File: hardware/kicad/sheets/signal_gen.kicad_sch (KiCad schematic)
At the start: 32 parts, among them U11 SG-8002CA-PH 25MHz, U12 AD9833BRMZ, U13 OPA1656ID, U14 AD633JRZ-R7, U15 MCP4921-E/SN, U16 LM4040DBZ-2.5, U17 OPA188ID

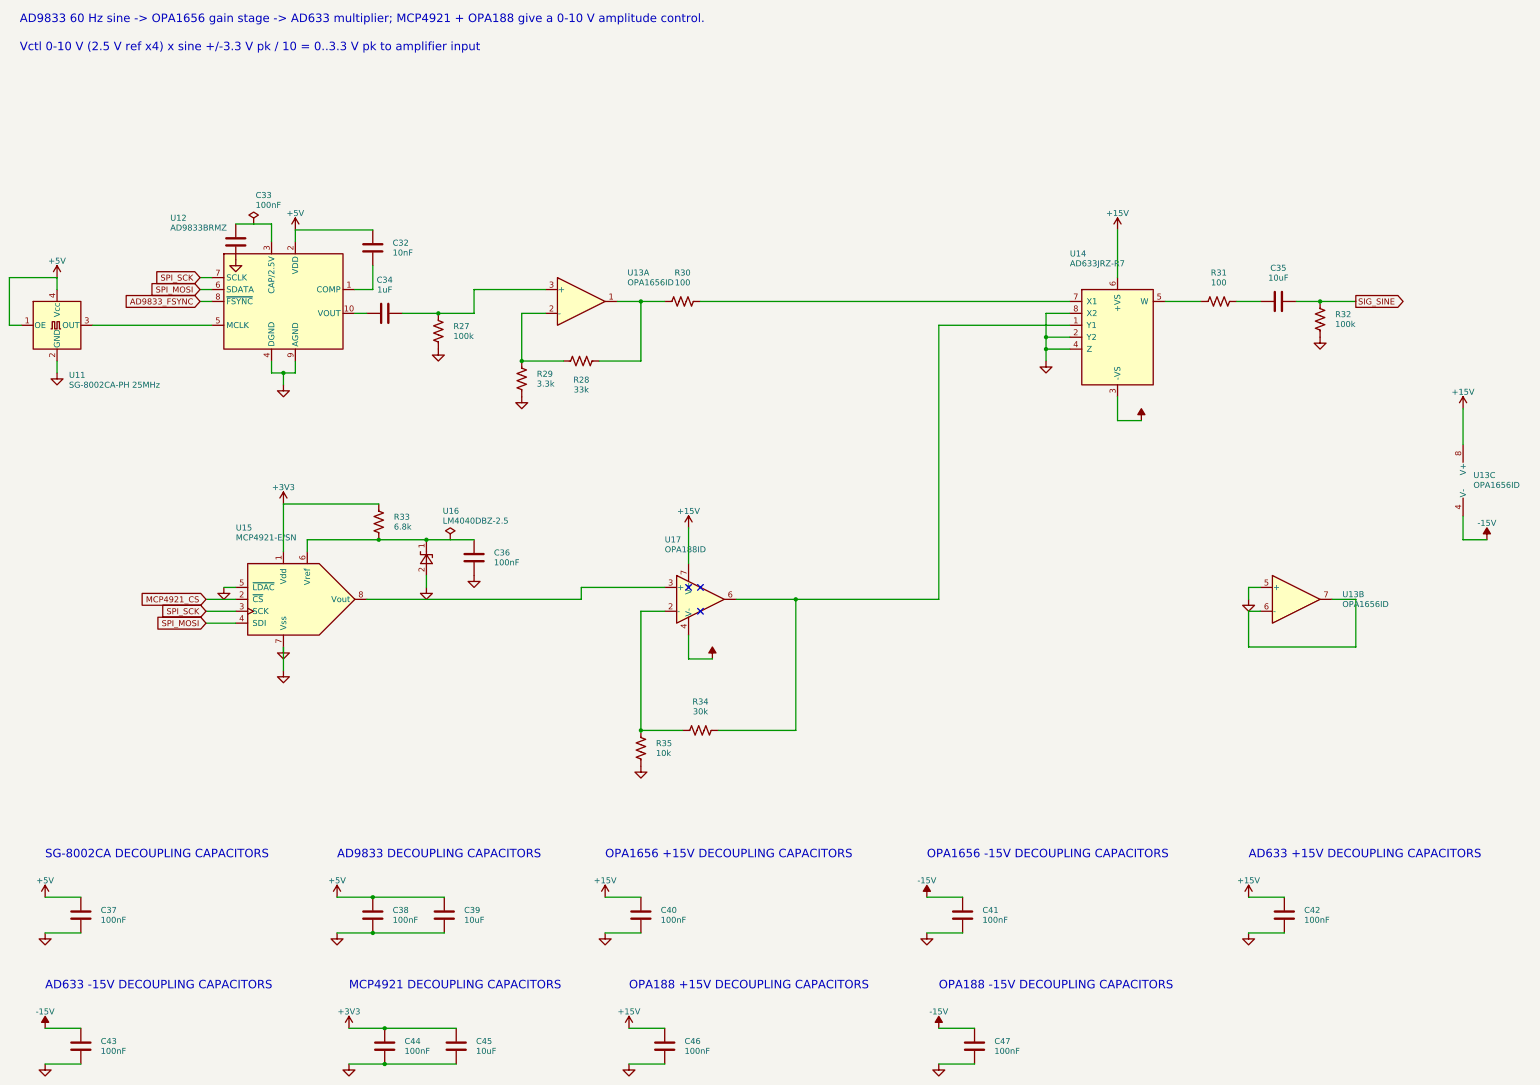
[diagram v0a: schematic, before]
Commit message: Fixing the UUID issues
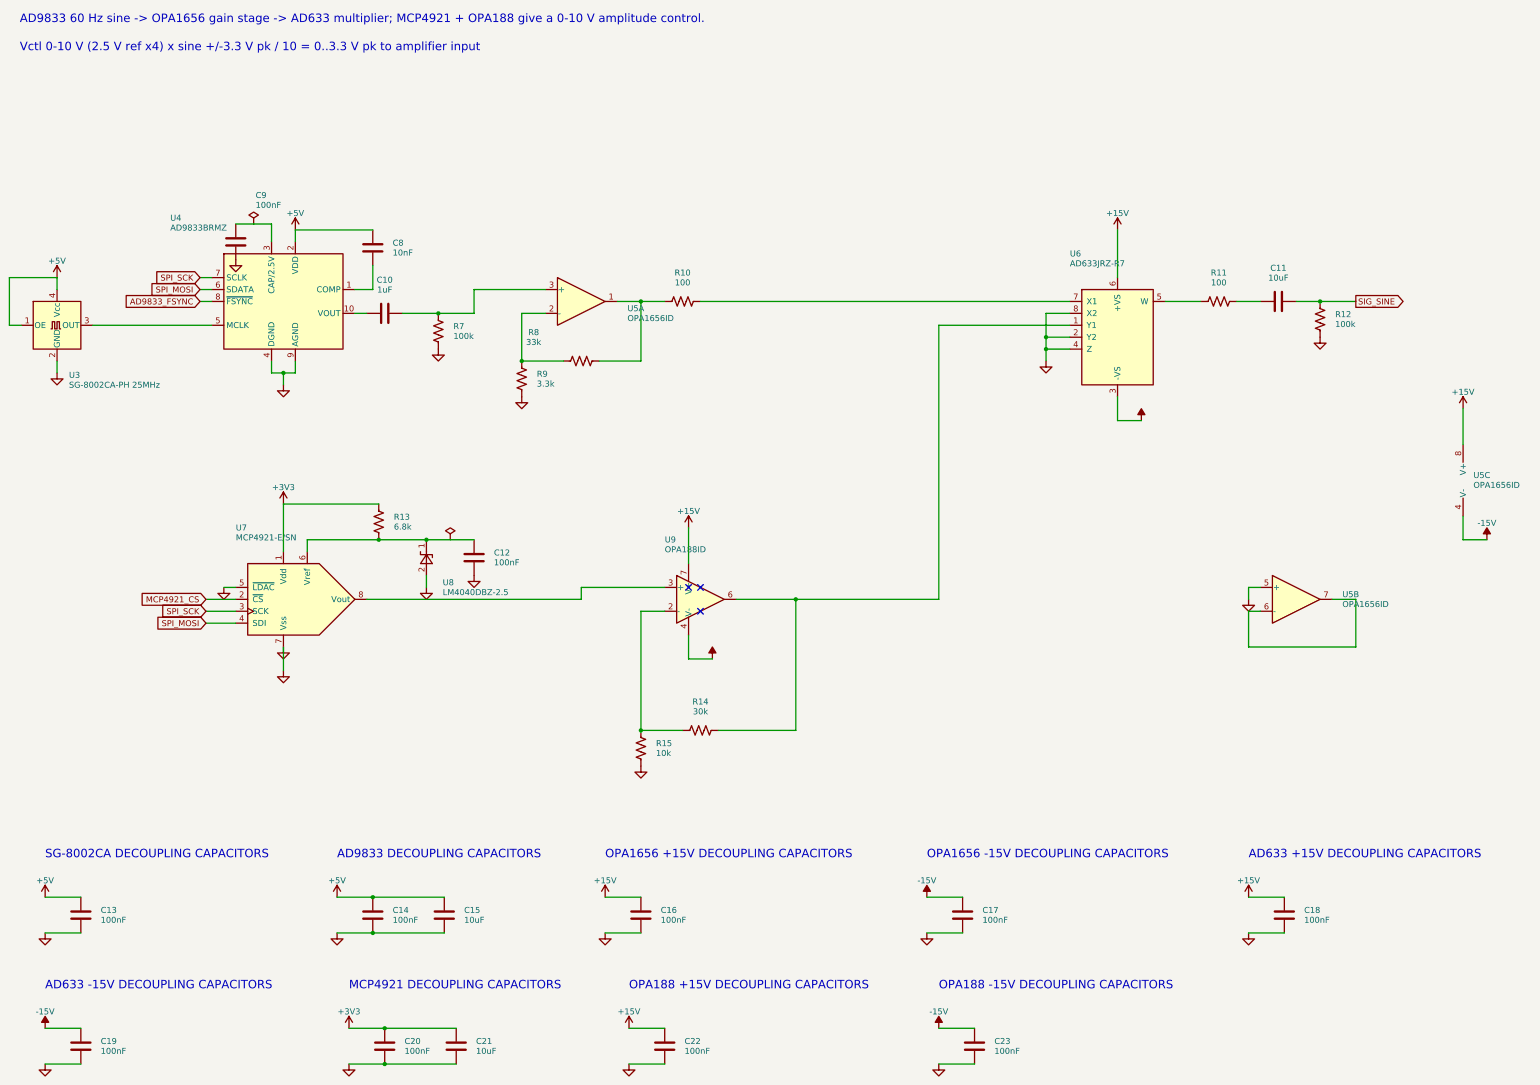
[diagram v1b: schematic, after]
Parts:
- removed C32: 10nF, Capacitor_SMD:C_0603_1608Metric, symbol Device:C
- removed C33, C36, C37, C38, C40, C41, C42, C43, C44, C46, C47: 100nF, Capacitor_SMD:C_0603_1608Metric, symbol Device:C
- removed C34: 1uF, Capacitor_SMD:C_0805_2012Metric, symbol Device:C
- removed C35, C39, C45: 10uF, Capacitor_SMD:C_0805_2012Metric, symbol Device:C
- removed R27, R32: 100k, Resistor_SMD:R_0603_1608Metric, symbol Device:R_US
- removed R28: 33k, Resistor_SMD:R_0603_1608Metric, symbol Device:R_US
- removed R29: 3.3k, Resistor_SMD:R_0603_1608Metric, symbol Device:R_US
- removed R30, R31: 100, Resistor_SMD:R_0603_1608Metric, symbol Device:R_US
- removed R33: 6.8k, Resistor_SMD:R_0603_1608Metric, symbol Device:R_US
- removed R34: 30k, Resistor_SMD:R_0603_1608Metric, symbol Device:R_US
- removed R35: 10k, Resistor_SMD:R_0603_1608Metric, symbol Device:R_US
- removed U11: SG-8002CA-PH 25MHz, Oscillator:Oscillator_SMD_SeikoEpson_SG8002CA-4Pin_7.0x5.0mm, symbol Oscillator:SG-8002CA
- removed U12: AD9833BRMZ, Package_SO:MSOP-10_3x3mm_P0.5mm, symbol Interface:AD9833xRM
- removed U13: OPA1656ID, Package_SO:SOIC-8_3.9x4.9mm_P1.27mm, symbol Amplifier_Operational:OPA1656ID
- removed U14: AD633JRZ-R7, Package_SO:SOIC-8_3.9x4.9mm_P1.27mm, symbol cryocooler:AD633JRZ-R7
- removed U15: MCP4921-E/SN, Package_SO:SOIC-8_3.9x4.9mm_P1.27mm, symbol Analog_DAC:MCP4921
- removed U16: LM4040DBZ-2.5, Package_TO_SOT_SMD:SOT-23, symbol Reference_Voltage:LM4040DBZ-2.5
- removed U17: OPA188ID, Package_SO:SOIC-8_3.9x4.9mm_P1.27mm, symbol Amplifier_Operational:OPA188xxD
- added C10: 1uF, Capacitor_SMD:C_0805_2012Metric, symbol Device:C
- added C11, C15, C21: 10uF, Capacitor_SMD:C_0805_2012Metric, symbol Device:C
- added C12, C13, C14, C16, C17, C18, C19, C20, C22, C23, C9: 100nF, Capacitor_SMD:C_0603_1608Metric, symbol Device:C
- added C8: 10nF, Capacitor_SMD:C_0603_1608Metric, symbol Device:C
- added R10, R11: 100, Resistor_SMD:R_0603_1608Metric, symbol Device:R_US
- added R12, R7: 100k, Resistor_SMD:R_0603_1608Metric, symbol Device:R_US
- added R13: 6.8k, Resistor_SMD:R_0603_1608Metric, symbol Device:R_US
- added R14: 30k, Resistor_SMD:R_0603_1608Metric, symbol Device:R_US
- added R15: 10k, Resistor_SMD:R_0603_1608Metric, symbol Device:R_US
- added R8: 33k, Resistor_SMD:R_0603_1608Metric, symbol Device:R_US
- added R9: 3.3k, Resistor_SMD:R_0603_1608Metric, symbol Device:R_US
- added U3: SG-8002CA-PH 25MHz, Oscillator:Oscillator_SMD_SeikoEpson_SG8002CA-4Pin_7.0x5.0mm, symbol Oscillator:SG-8002CA
- added U4: AD9833BRMZ, Package_SO:MSOP-10_3x3mm_P0.5mm, symbol Interface:AD9833xRM
- added U5: OPA1656ID, Package_SO:SOIC-8_3.9x4.9mm_P1.27mm, symbol Amplifier_Operational:OPA1656ID
- added U6: AD633JRZ-R7, Package_SO:SOIC-8_3.9x4.9mm_P1.27mm, symbol cryocooler:AD633JRZ-R7
- added U7: MCP4921-E/SN, Package_SO:SOIC-8_3.9x4.9mm_P1.27mm, symbol Analog_DAC:MCP4921
- added U8: LM4040DBZ-2.5, Package_TO_SOT_SMD:SOT-23, symbol Reference_Voltage:LM4040DBZ-2.5
- added U9: OPA188ID, Package_SO:SOIC-8_3.9x4.9mm_P1.27mm, symbol Amplifier_Operational:OPA188xxD
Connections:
- net +15V: now also C16.1, C18.1, C22.1, U5.8 (V+), U6.6 (+VS), U9.7 (V+)
- net +3V3: now also C20.1, C21.1, R13.1, U7.1 (Vdd)
- net +5V: now also C13.1, C14.1, C15.1, C8.1, U3.1 (OE), U3.4 (Vcc), U4.2 (VDD)
- net -15V: now also C17.1, C19.1, C23.1, U5.4 (V-), U6.3 (-VS), U9.4 (V-)
- net AD9833_FSYNC: now also U4.8 (~{FSYNC})
- net GND: now also C12.2, C13.2, C14.2, C15.2, C16.2, C17.2, C18.2, C19.2, C20.2, C21.2, C22.2, C23.2, C9.2, R12.2, R15.2, R7.2, R9.2, U3.2 (GND), U4.4 (DGND), U4.9 (AGND), U5.5 (+), U6.2 (Y2), U6.4 (Z), U6.8 (X2), U7.5 (~{LDAC}), U7.7 (Vss), U8.2 (A)
- net MCP4921_CS: now also U7.2 (~{CS})
- net SIG_SINE: now also C11.2, R12.1
- net SPI_MOSI: now also U4.6 (SDATA), U7.4 (SDI)
- net SPI_SCK: now also U4.7 (SCLK), U7.3 (SCK)
- new net: C10.2, R7.1, U5.3 (+)
- new net: C12.1, R13.2, U7.6 (Vref), U8.1 (K)
- new net: U7.8 (Vout), U9.3 (+)
- new net: R14.1, R15.1, U9.2 (-)
- new net: R14.2, U6.1 (Y1), U9.6
- new net: C10.1, U4.10 (VOUT)
- new net: R10.1, R8.2, U5.1
- new net: R8.1, R9.1, U5.2 (-)
- new net: U5.6 (-), U5.7
- new net: C8.2, U4.1 (COMP)
- new net: C9.1, U4.3 (CAP/2.5V)
- new net: U3.3 (OUT), U4.5 (MCLK)
- new net: R11.1, U6.5 (W)
- new net: C11.1, R11.2
- new net: R10.2, U6.7 (X1)
